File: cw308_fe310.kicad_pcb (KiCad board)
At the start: 2 copper layers, 56 x 67 mm, 53 parts, among them J1 CW308T_CONNBOARD, J2 Conn_01x03, J3 Conn_01x03, J4 Conn_02x05_Odd_Even, J5 10118192-0001LF, U1 IS25LP128, U2 SN74LVC1G07DBVR, U3 SN74LVC1G07DBVR, U4 FE310-G000, U5 FT2232HL-REEL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

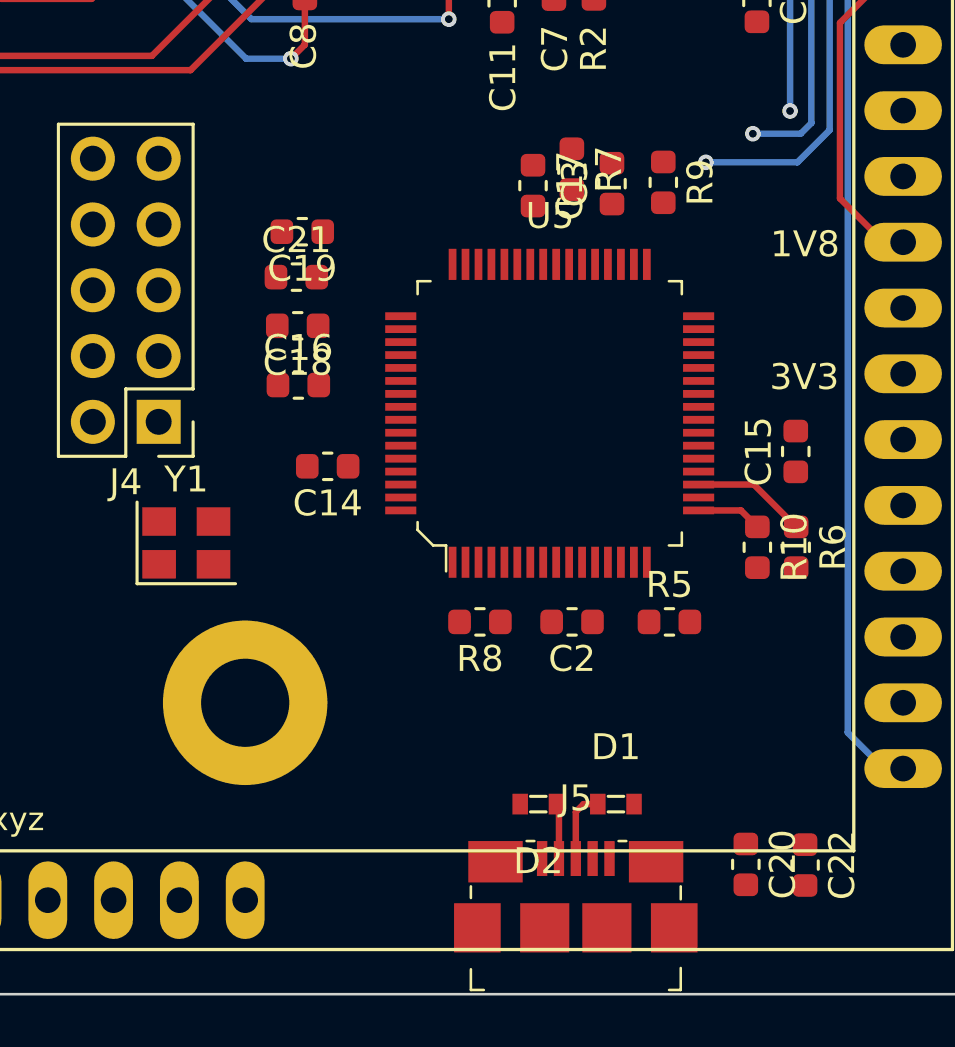
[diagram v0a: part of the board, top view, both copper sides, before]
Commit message: added missing footprints, fixed netlist issue with missing pads for cw connector
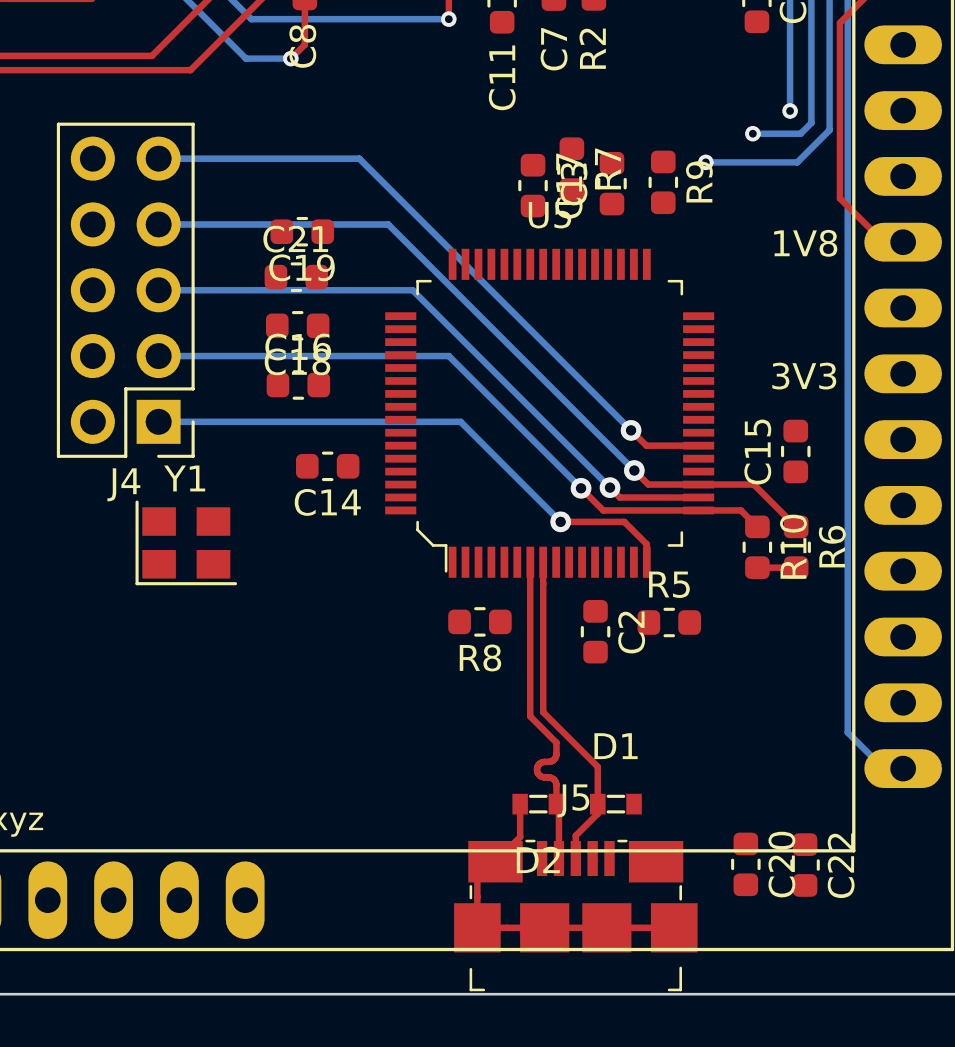
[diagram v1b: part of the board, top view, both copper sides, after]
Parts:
- moved C2 0.98 mm to (158.1, 110.0), turned to 270 degrees
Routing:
- net FT_RST: track 0.00 -> 25.4 mm, vias 0 -> 1
- net FT_JTAG_TMS: track 4.44 -> 29.4 mm, vias 0 -> 1
- net FT_JTAG_TDO: track 0.00 -> 24.2 mm, vias 0 -> 1
- net FT_JTAG_TDI: track 2.53 -> 25.8 mm, vias 0 -> 1
- net FT_JTAG_TCK: track 0.00 -> 21.5 mm, vias 0 -> 1
- net GND: track 40.1 -> 54.8 mm
- net DM: track 2.14 -> 12.7 mm
- net DP: track 2.77 -> 12.7 mm

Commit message: done routing
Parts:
- moved C27 68.4 mm to (159.5, 111.3)
- moved J3 67.1 mm to (126.9, 71.2), turned to 90 degrees
- moved J2 64.5 mm to (126.9, 67.5), turned to 90 degrees
- moved FB2 64.1 mm to (159.6, 107.9)
- moved C23 63.8 mm to (161.0, 97.6), turned to 180 degrees
- moved FB1 62.6 mm to (161.1, 102.6)
- moved C25 60.0 mm to (159.5, 109.8)
- moved C24 58.7 mm to (161.0, 100.8)
- moved C26 58.6 mm to (161.0, 99.2)
- moved R9 23.2 mm to (140.6, 104.3)
- moved C19 21.5 mm to (148.2, 116.0)
- moved C17 19.8 mm to (141.4, 106.6), turned to 180 degrees
- moved R7 19.3 mm to (142.2, 104.3)
- moved C3 18.4 mm to (142.2, 100.8)
- moved C21 18.2 mm to (148.2, 114.5), turned to 180 degrees
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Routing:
- net +3V3: track 96.7 -> 260.6 mm, vias 5 -> 8
- net GND: track 54.8 -> 200.3 mm, vias 5 -> 23
- net UFO.RST: track 0.00 -> 100.5 mm
- net JTAG_TRST: track 0.00 -> 60.7 mm, vias 0 -> 1
- net JTAG_TMS: track 0.00 -> 52.0 mm, vias 0 -> 2
- net JTAG_TDO: track 0.00 -> 50.1 mm, vias 0 -> 2
- net JTAG_TDI: track 0.00 -> 48.6 mm, vias 0 -> 1
- net FT_TX: track 0.00 -> 46.6 mm, vias 0 -> 2
- net FT_RX: track 0.00 -> 44.9 mm, vias 0 -> 1
- net JTAG_TCK: track 0.00 -> 44.5 mm
- net VCORE_FT: track 0.00 -> 40.2 mm, vias 0 -> 2
- net FT_JTAG_TMS: track 29.4 -> 8.52 mm
- net LED1: track 33.0 -> 53.9 mm
- net LED2: track 39.0 -> 58.7 mm
- net FT_RST: track 25.4 -> 9.03 mm, vias 1 -> 0
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- removed copper zone on B.Cu, net GND

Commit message: minor changes
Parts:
- removed G***: LOGO, cw308_fe310:logo
- removed J3: Conn_01x03, Connector_PinHeader_2.54mm:PinHeader_1x03_P2.54mm_Vertical
- J2: value Conn_01x03 -> Conn_02x03_Odd_Even; footprint Connector_PinHeader_2.54mm:PinHeader_1x03_P2.54mm_Vertical -> Connector_PinHeader_2.54mm:PinHeader_2x03_P2.54mm_Vertical
- moved J2 2.07 mm to (126.7, 69.6)
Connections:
- J2 pad 1: GPIO1 -> GPIO2
- J2 pad 2: RX -> GPIO1
- J2 pad 3: FT_TX -> TX
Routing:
- net FT_RX: track 44.9 -> 46.4 mm
- net GPIO2: track 17.1 -> 18.4 mm
- net TX: track 29.5 -> 30.0 mm
- added copper zone on B.Cu, net GND
- removed copper zone on F.Cu, net GND
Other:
- board text added: "RX"
- board text added: "Rev 0.2"
- board text added: "TCK TDI TDO TMS TRST"
- board text added: "TX"
- board text removed: "R"
- board text removed: "Rev 0.1"
- board text removed: "T"
- board text removed: "X"

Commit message: order made
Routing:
- added copper zone on B.Cu, net (none)
- added copper zone on F.Cu, net GND
- removed copper zone on B.Cu, net GND
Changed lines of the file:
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@@
   (page A4)
   (layers
-    (0 F.Cu signal hide)
-    (31 B.Cu signal hide)
+    (0 F.Cu signal)
+    (31 B.Cu signal)
     (32 B.Adhes user hide)
     (33 F.Adhes user hide)
@@
     (visible_elements FFFFFFFF)
     (pcbplotparams
-      (layerselection 0x010fc_ffffffff)
+      (layerselection 0x010f0_ffffffff)
       (usegerberextensions false)
-      (usegerberattributes false)
+      (usegerberattributes true)
       (usegerberadvancedattributes false)
       (creategerberjobfile false)
       (excludeedgelayer true)
-      (linewidth 0.100000)
+      (linewidth 0.150000)
       (plotframeref false)
       (viasonmask false)
@@
   (segment (start 151.76246 94.0816) (end 152.47112 93.37294) (width 0.25) (layer F.Cu) (net 113))
   (segment (start 153.85542 93.37294) (end 154.572601 92.655759) (width 0.25) (layer F.Cu) (net 113))
-  (zone (net 1) (net_name GND) (layer B.Cu) (hatch edge 0.508)
+  (zone (net 1) (net_name GND) (layer F.Cu) (hatch edge 0.508)
     (connect_pads (clearance 0.508))
     (min_thickness 0.254)
@@
       )
     )
+  )
+  (zone (net 0) (net_name "") (layer B.Cu) (hatch edge 0.508)
+    (connect_pads (clearance 0.508))
+    (min_thickness 0.254)
+    (fill yes (arc_segments 16) (thermal_gap 0.508) (thermal_bridge_width 0.508))
+    (polygon
+      (pts
+        (xy 117.9957 56.9976) (xy 117.9957 124.0028) (xy 174.0027 124.0028) (xy 174.0027 56.9976)
+      )
+    )

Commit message: reloaded netlist, re-routed uforst, regenerated fill zones
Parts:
- C20, C22: value 0.1uF -> 27pF
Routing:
- net UFO.RST: track 100.3 -> 86.6 mm, vias 0 -> 1
